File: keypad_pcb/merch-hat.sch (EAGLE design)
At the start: 15 parts

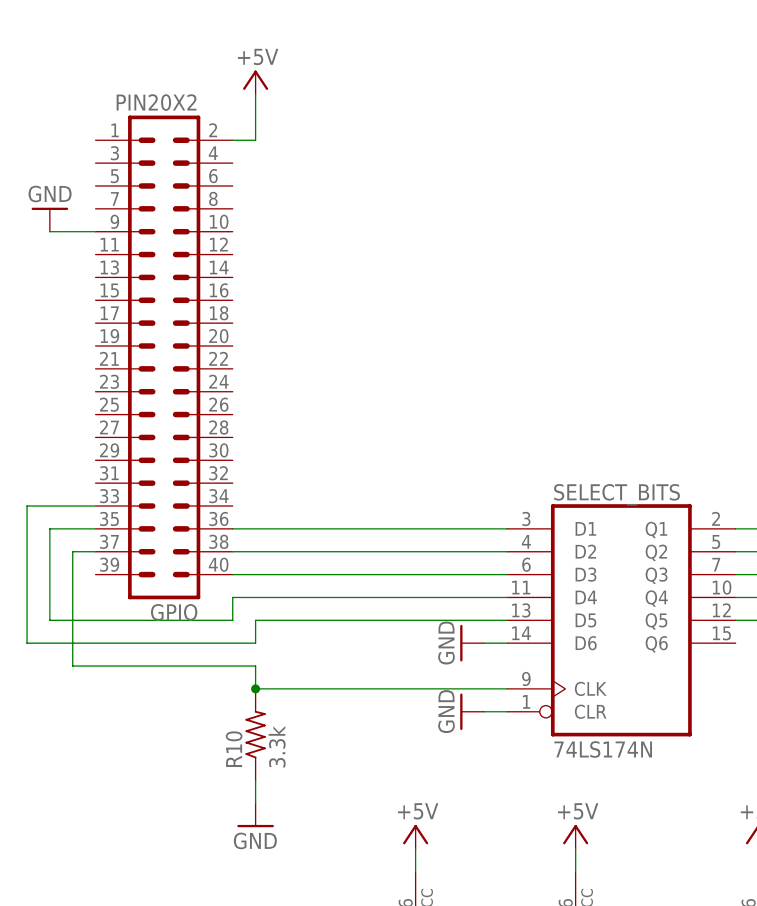
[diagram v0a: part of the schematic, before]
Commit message: update pcbs to remove clear bug on 74174 chip
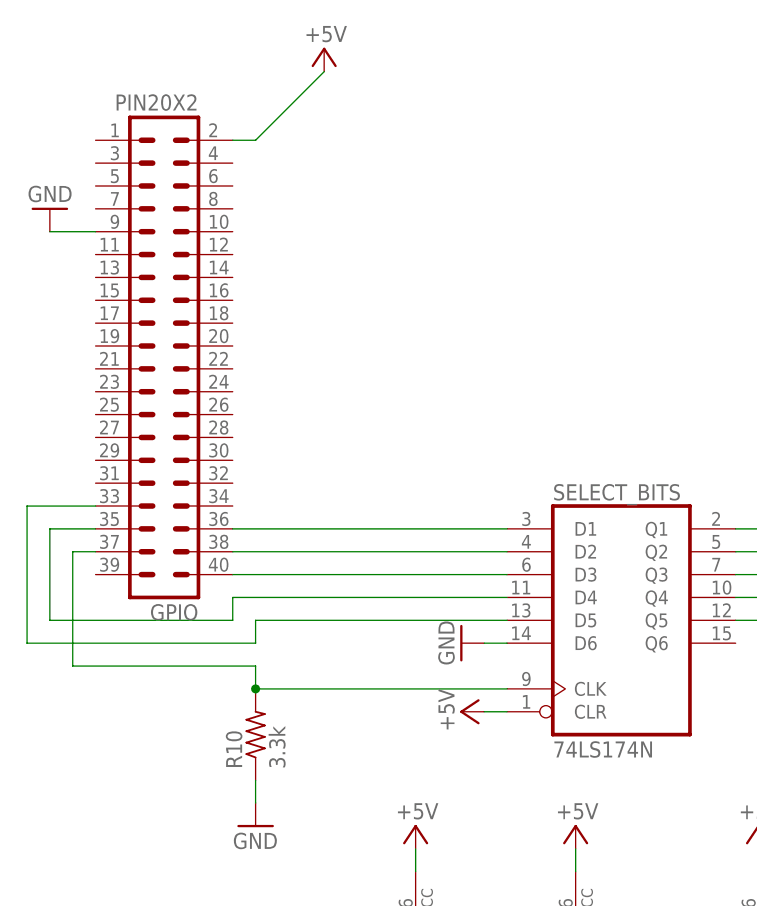
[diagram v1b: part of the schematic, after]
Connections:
- net +5V: now also SELECT_BITSA.CLR
- net GND: no longer SELECT_BITSA.CLR
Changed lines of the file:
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@@
 <part name="GND1" library="supply1" deviceset="GND" device=""/>
 <part name="GND2" library="supply1" deviceset="GND" device=""/>
-<part name="GND3" library="supply1" deviceset="GND" device=""/>
 <part name="P+2" library="supply1" deviceset="+5V" device=""/>
 <part name="P+4" library="supply1" deviceset="+5V" device=""/>
@@
 <part name="R10" library="resistor" deviceset="R-US_" device="0207/10" value="3.3k"/>
 <part name="GND9" library="supply1" deviceset="GND" device=""/>
+<part name="P+9" library="supply1" deviceset="+5V" device=""/>
 </parts>
 <sheets>
@@
 <instance part="FRAME1" gate="G$1" x="0" y="0"/>
 <instance part="GND10" gate="1" x="27.94" y="177.8" rot="R180"/>
-<instance part="P+1" gate="1" x="50.8" y="193.04" smashed="yes">
-<attribute name="VALUE" x="53.34" y="195.58" size="1.778" layer="96" rot="R180"/>
+<instance part="P+1" gate="1" x="58.42" y="195.58" smashed="yes">
+<attribute name="VALUE" x="60.96" y="198.12" size="1.778" layer="96" rot="R180"/>
 </instance>
 <instance part="ROW_MUX" gate="A" x="147.32" y="109.22" rot="R270"/>
@@
 <instance part="GND1" gate="1" x="132.08" y="127" rot="R180"/>
 <instance part="GND2" gate="1" x="73.66" y="129.54" rot="R270"/>
-<instance part="GND3" gate="1" x="73.66" y="121.92" rot="R270"/>
 <instance part="P+2" gate="1" x="144.78" y="127" smashed="yes">
 <attribute name="VALUE" x="147.32" y="129.54" size="1.778" layer="96" rot="R180"/>
@@
 <instance part="R10" gate="G$1" x="50.8" y="119.38" rot="R90"/>
 <instance part="GND9" gate="1" x="50.8" y="109.22"/>
+<instance part="P+9" gate="1" x="73.66" y="121.92" smashed="yes" rot="R90">
+<attribute name="VALUE" x="71.12" y="124.46" size="1.778" layer="96" rot="R270"/>
+</instance>
 </instances>
 <busses>
@@
 </segment>
 <segment>
-<pinref part="SELECT_BITS" gate="A" pin="CLR"/>
-<pinref part="GND3" gate="1" pin="GND"/>
-<wire x1="78.74" y1="121.92" x2="76.2" y2="121.92" width="0.1524" layer="91"/>
-</segment>
-<segment>
 <pinref part="ROW_MUX" gate="P" pin="GND"/>
 <pinref part="GND5" gate="1" pin="GND"/>
@@
 <pinref part="P+1" gate="1" pin="+5V"/>
 <wire x1="48.26" y1="185.42" x2="50.8" y2="185.42" width="0.1524" layer="91"/>
-<wire x1="50.8" y1="185.42" x2="50.8" y2="190.5" width="0.1524" layer="91"/>
+<wire x1="50.8" y1="185.42" x2="58.42" y2="193.04" width="0.1524" layer="91"/>
 </segment>
 <segment>
@@
 <wire x1="106.68" y1="106.68" x2="106.68" y2="104.14" width="0.1524" layer="91"/>
 </segment>
+<segment>
+<pinref part="SELECT_BITS" gate="A" pin="CLR"/>
+<wire x1="78.74" y1="121.92" x2="76.2" y2="121.92" width="0.1524" layer="91"/>
+<pinref part="P+9" gate="1" pin="+5V"/>
+</segment>
 </net>
